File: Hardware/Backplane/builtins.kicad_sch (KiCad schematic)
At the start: 28 parts, among them J1001 Conn_01x06, J1002 Conn_01x06, J1003 Conn_01x06, J1004 Conn_01x06, Q1001 NMOS, SW1001 SW_Push, U1001 LTC6930CMS8-8.00#PBF, U1002 DS1307Z+, Y1001 Crystal

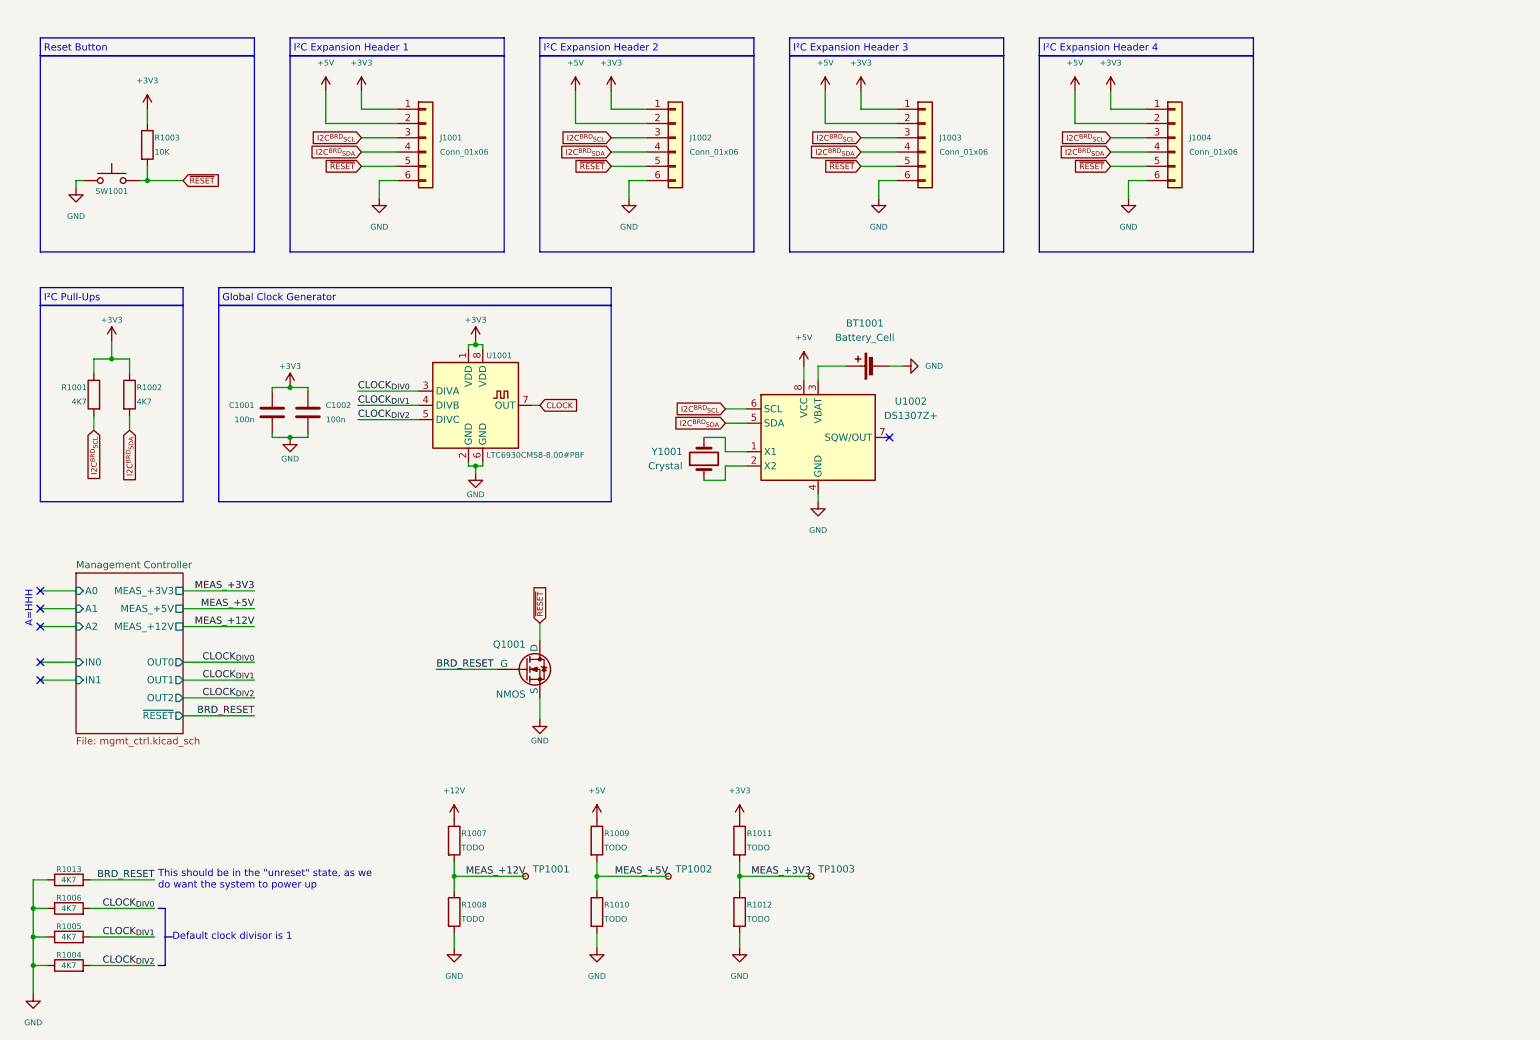
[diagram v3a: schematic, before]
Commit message: Cleans up schematic, adds clean RESET gating
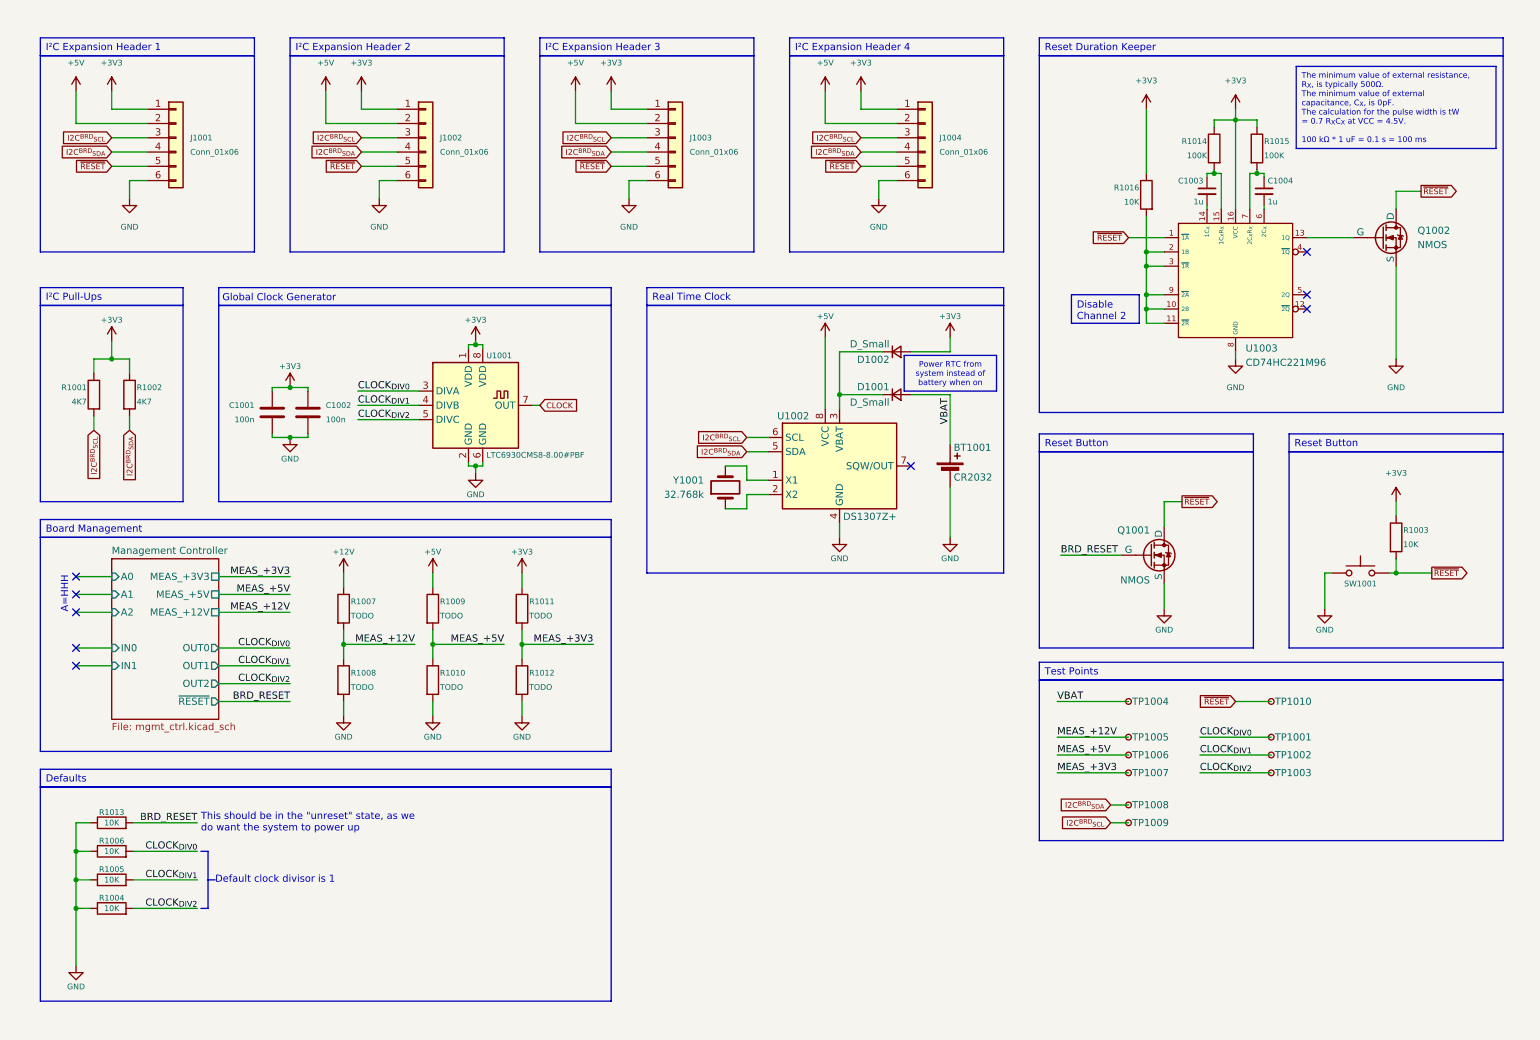
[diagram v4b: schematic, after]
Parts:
- added C1003, C1004: 1u, Capacitor_SMD:C_0603_1608Metric, symbol Device:C_Small
- added D1001, D1002: D_Small, symbol Device:D_Small
- added Q1002: NMOS, Package_TO_SOT_SMD:SOT-23, symbol Simulation_SPICE:NMOS
- added R1014, R1015: 100K, Resistor_SMD:R_0603_1608Metric, symbol Device:R
- added R1016: 10K, Resistor_SMD:R_0603_1608Metric, symbol Device:R
- added TP1004, TP1005, TP1006, TP1007, TP1008, TP1009, TP1010: TestPoint_Small, TestPoint:TestPoint_Pad_D1.0mm, symbol Connector:TestPoint_Small
- added U1003: CD74HC221M96, symbol Symbol Library:CD74HC221M96
- BT1001: value Battery_Cell -> CR2032
- R1004, R1005, R1006, R1013: value 4K7 -> 10K
- Y1001: value Crystal -> 32.768k
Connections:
- net +3V3: now also D1002.2 (A), R1014.1, R1015.1, R1016.1, U1003.16 (VCC)
- net CLOCK_{DIV0}: now also TP1001.1
- net CLOCK_{DIV1}: now also TP1002.1
- net CLOCK_{DIV2}: now also TP1003.1
- net GND: now also Q1002.3 (S), U1003.8 (GND)
- net I2C^{BRD}_{SCL}: now also TP1009.1
- net I2C^{BRD}_{SDA}: now also TP1008.1
- net MEAS_+12V: now also TP1005.1; no longer TP1001.1
- net MEAS_+3V3: now also TP1007.1; no longer TP1003.1
- net MEAS_+5V: now also TP1006.1; no longer TP1002.1
- net ~{RESET}: now also Q1002.1 (D), TP1010.1, U1003.1 (~{1A})
- net at U1002.3 (VBAT): now also D1001.1 (K), D1002.1 (K); no longer BT1001.1 (+)
- new net: Q1002.2 (G), U1003.13 (1Q)
- new net: R1016.2, U1003.10 (2B), U1003.11 (~{2R}), U1003.2 (1B), U1003.3 (~{1R}), U1003.9 (~{2A})
- new net: C1003.2, U1003.14 (1C_{X})
- new net: C1003.1, R1014.2, U1003.15 (1C_{X}R_{X})
- new net: C1004.2, U1003.6 (2C_{X})
- new net: C1004.1, R1015.2, U1003.7 (2C_{X}R_{X})
- new net VBAT: BT1001.1 (+), D1001.2 (A), TP1004.1
- no-connect marks 6 -> 9
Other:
- note removed: "I²C Expansion Header 1"
- note removed: "I²C Expansion Header 2"
- note removed: "I²C Expansion Header 3"
- note removed: "I²C Expansion Header 4"
- note removed: "I²C Pull-Ups"
- note removed: "Reset Button"
- company: (none) -> Ashet Technologies
- moved on the sheet: BT1001, J1001, J1002, J1003, J1004, Q1001, R1003, R1004, R1005, R1006, R1007, R1008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

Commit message: Updates backplane: Improves voltage measurement dividers, replaces DS1307+ RTC with a much cheaper one, replaces 8 MHz global clock with 48 MHz global clock
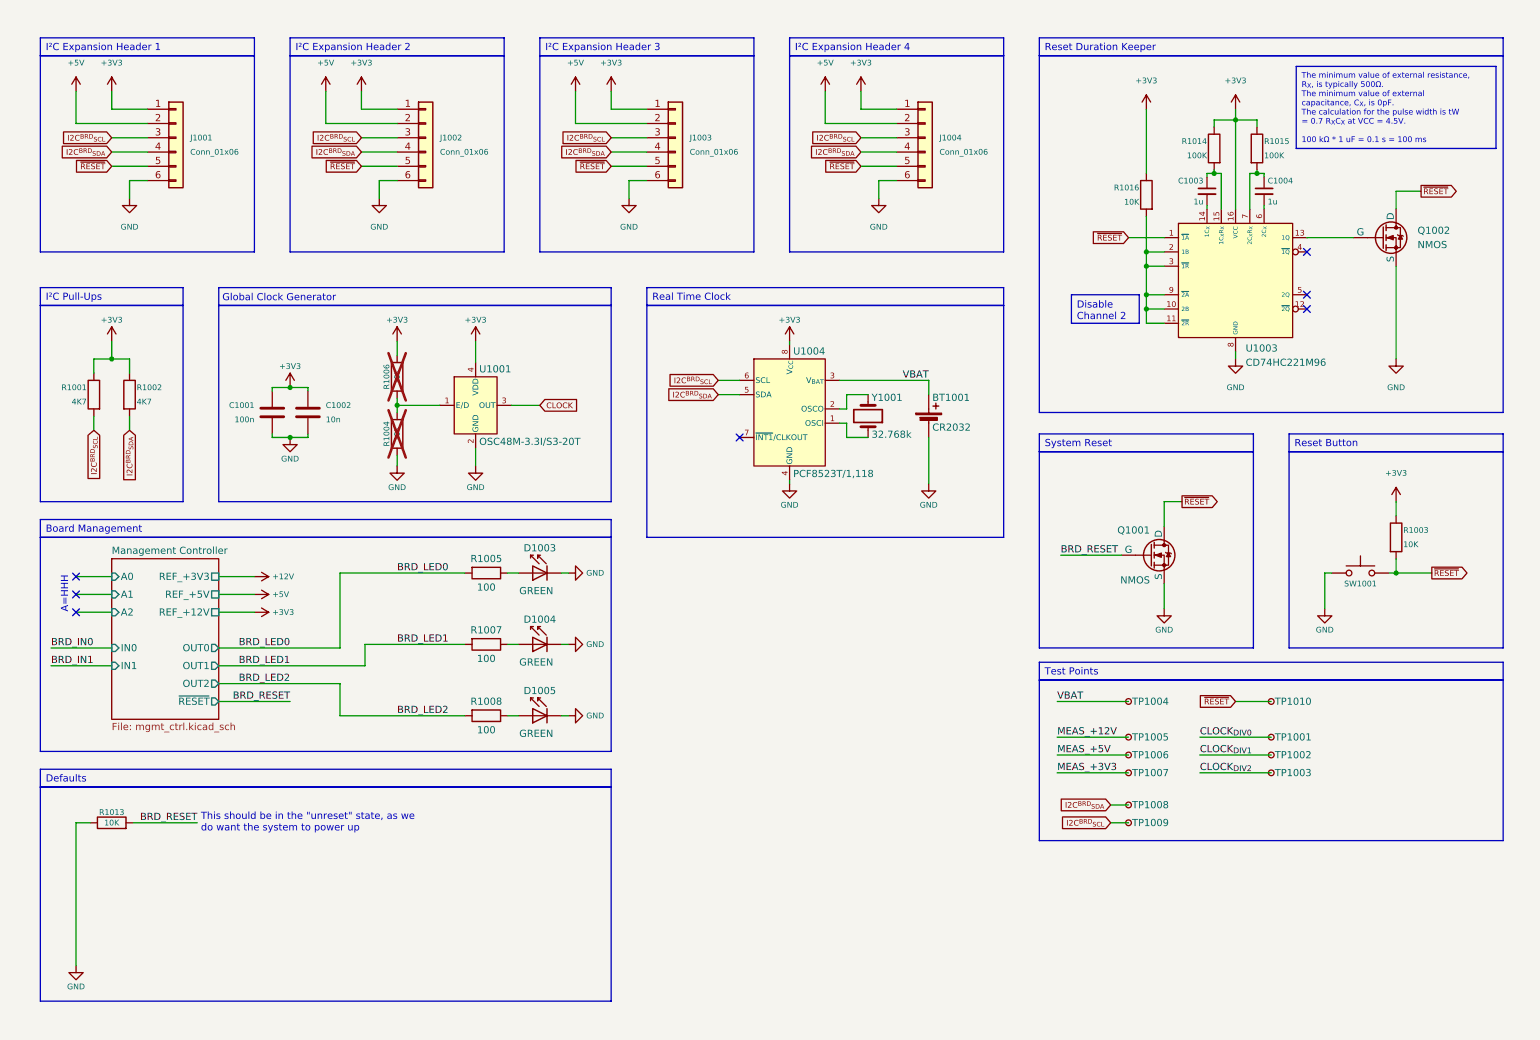
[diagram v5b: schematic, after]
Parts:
- removed D1001, D1002: D_Small, symbol Device:D_Small
- removed R1009, R1010, R1011, R1012: TODO, Resistor_SMD:R_0603_1608Metric, symbol Device:R
- removed U1001: LTC6930CMS8-8.00#PBF, symbol Home Computer:LTC6930CMS8-8.00#PBF
- removed U1002: DS1307Z+, Package_SO:SOIC-8_3.9x4.9mm_P1.27mm, symbol Timer_RTC:DS1307Z+
- added D1003, D1004, D1005: GREEN, LED_SMD:LED_0603_1608Metric, symbol LED:LD271
- added U1001: OSC48M-3.3I/S3-20T, symbol Home Computer:OSC48M-3.3I/S3-20T
- added U1004: PCF8523T/1,118, Home Computer:PCF8523T1,118, symbol Home Computer:PCF8523T/1
- C1002: value 100n -> 10n
- R1004, R1006: now not fitted; now left out of the parts list
- R1005: value 10K -> 100; footprint Resistor_SMD:R_0603_1608Metric -> (none)
- R1007, R1008: value TODO -> 100; footprint Resistor_SMD:R_0603_1608Metric -> (none)
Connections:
- net +12V: no longer R1007.1
- net +3V3: now also R1006.2, U1001.4 (VDD), U1004.8 (V_{CC})
- net CLOCK: now also U1001.3 (OUT)
- net CLOCK_{DIV0}: no longer R1006.2
- net CLOCK_{DIV1}: no longer R1005.2
- net CLOCK_{DIV2}: no longer R1004.2
- net GND: now also D1003.1 (K), D1004.1 (K), D1005.1 (K), U1001.2 (GND), U1004.4 (GND); no longer R1005.1, R1006.1, R1008.2
- net I2C^{BRD}_{SCL}: now also U1004.6 (SCL)
- net I2C^{BRD}_{SDA}: now also U1004.5 (SDA)
- net MEAS_+12V: no longer R1007.2, R1008.1
- net VBAT: now also U1004.3 (V_{BAT})
- net at Y1001.1: now also U1004.1 (OSCI)
- net at Y1001.2: now also U1004.2 (OSCO)
- new net: R1004.2, R1006.1, U1001.1 (E/D)
- new net: D1003.2 (A), R1005.1
- new net: D1004.2 (A), R1007.1
- new net: D1005.2 (A), R1008.1
- new net BRD_LED0: R1005.2
- new net BRD_LED1: R1007.2
- new net BRD_LED2: R1008.2
- no-connect marks 9 -> 7
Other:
- sheet Management Controller ports: added REF_+12V, REF_+3V3, REF_+5V; removed MEAS_+12V, MEAS_+3V3, MEAS_+5V
- note removed: "Default clock divisor is 1"
- moved on the sheet: BT1001, Y1001

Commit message: Upgrades power-on reset system to be close to bullet-proof by having a power-good coupled mono flop that continues holding reset after PG goes high for some time
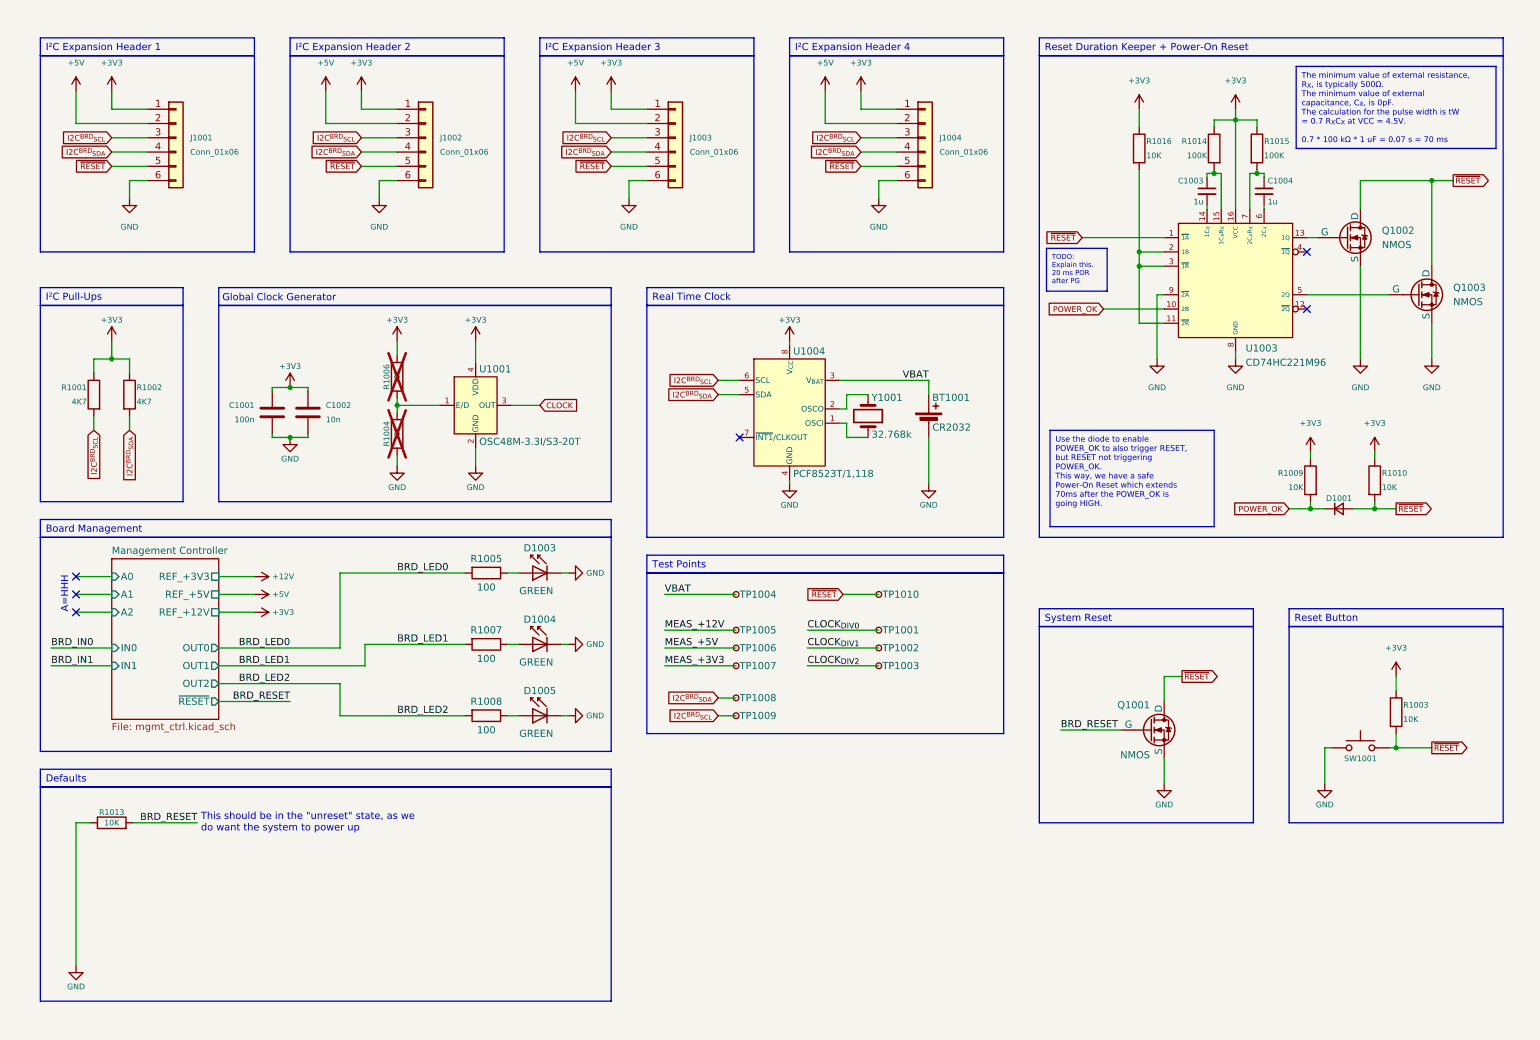
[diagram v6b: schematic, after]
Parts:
- added D1001: Something Short-Circuit Safe, Diode_SMD:D_1206_3216Metric, symbol Device:D_Small
- added Q1003: NMOS, Package_TO_SOT_SMD:SOT-23, symbol Simulation_SPICE:NMOS
- added R1009, R1010: 10K, Resistor_SMD:R_0603_1608Metric, symbol Device:R
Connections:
- net +3V3: now also R1009.1, R1010.1
- net GND: now also U1003.9 (~{2A}), Q1003.3 (S)
- net ~{RESET}: now also D1001.2 (A), Q1003.1 (D), R1010.2
- net at R1016.2, U1003.11 (~{2R}), U1003.2 (1B)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: no longer U1003.10 (2B), U1003.9 (~{2A})
- net at U1003.5 (2Q): now also Q1003.2 (G)
- new net POWER_OK: D1001.1 (K), R1009.2, U1003.10 (2B)
- no-connect marks 7 -> 6
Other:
- moved on the sheet: Q1001, Q1002, R1003, R1016, SW1001, TP1001, TP1002, TP1003, TP1004, TP1005, TP1006, TP1007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
